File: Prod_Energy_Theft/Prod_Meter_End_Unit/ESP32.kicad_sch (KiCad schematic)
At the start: 24 parts, among them J8 U.FL-R-SMT_01_, U2 ESP32-C6-MINI-1, U4 CP2102N-Axx-xQFN20, U6 USBLC6-2SC6, U8 E32-433T20S

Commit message: PCB
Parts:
- C15, C17: footprint Footprints.kicad_mod:T491A -> Capacitor_SMD:C_0805_2012Metric
- D7, D8: footprint Footprints:LEDC2012X120N -> theftdetection:LEDC2012X120N
- J8: footprint U.FL-R-SMT_01_:HRS_U.FL-R-SMT_01_ -> theftdetection:HRS_U.FL-R-SMT_01_
- U4: footprint Package_DFN_QFN:SiliconLabs_QFN-20-1EP_3x3mm_P0.5mm -> theftdetection:IC_CP2102N-A01-GQFN20
- U8: footprint E32-433T20S:MODULE_E32-433T20S -> theftdetection:MODULE_E32-433T20S
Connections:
- net 3.3V is gone; now on net +3.3V: D7.2 (A), D8.2 (A)
- net MCB_CTRL renamed MCB_SET
- net MCB_CTRL_D renamed MCB_RESET
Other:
- sheet MCB_TD ports: added MCB_RESET, MCB_SET; removed MCB_CTRL, MCB_CTRL_D
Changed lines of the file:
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@@
 		)
 	)
-	(label "MCB_CTRL_D"
+	(label "MCB_RESET"
 		(at 270.51 147.32 0)
 		(effects
@@
 		)
 	)
-	(label "MCB_CTRL"
+	(label "MCB_SET"
 		(at 270.51 151.13 0)
 		(effects
@@
 		)
 	)
-	(label "MCB_CTRL_D"
+	(label "MCB_RESET"
 		(at 176.53 113.03 180)
 		(effects
@@
 		)
 	)
-	(label "MCB_CTRL"
+	(label "MCB_SET"
 		(at 176.53 110.49 180)
 		(effects
@@
 			)
 		)
-		(property "Footprint" "Footprints.kicad_mod:T491A"
+		(property "Footprint" "Capacitor_SMD:C_0805_2012Metric"
 			(at 118.4148 157.48 0)
 			(effects
@@
 			)
 		)
-		(property "Footprint" "U.FL-R-SMT_01_:HRS_U.FL-R-SMT_01_"
+		(property "Footprint" "theftdetection:HRS_U.FL-R-SMT_01_"
 			(at 36.83 160.02 0)
 			(effects
@@
 			)
 		)
-		(property "Footprint" "E32-433T20S:MODULE_E32-433T20S"
+		(property "Footprint" "theftdetection:MODULE_E32-433T20S"
 			(at 78.74 154.94 0)
 			(effects
@@
 			)
 		)
-		(property "Footprint" "Footprints:LEDC2012X120N"
+		(property "Footprint" "theftdetection:LEDC2012X120N"
 			(at 138.43 181.28 0)
 			(effects
@@
 			)
 		)
-		(property "Value" "3.3V"
+		(property "Value" "+3.3V"
 			(at 144.78 82.55 0)
 			(do_not_autoplace yes)
@@
 			)
 		)
-		(property "Footprint" "Footprints.kicad_mod:T491A"
+		(property "Footprint" "Capacitor_SMD:C_0805_2012Metric"
 			(at 71.12 29.5148 0)
 			(effects
@@
 			)
 		)
-		(property "Footprint" "Package_DFN_QFN:SiliconLabs_QFN-20-1EP_3x3mm_P0.5mm"
+		(property "Footprint" "theftdetection:IC_CP2102N-A01-GQFN20"
 			(at 118.11 104.14 0)
 			(effects
@@
 			)
 		)
-		(property "Footprint" "Footprints:LEDC2012X120N"
+		(property "Footprint" "theftdetection:LEDC2012X120N"
 			(at 138.43 191.44 0)
 			(effects
@@
 			)
 		)
-		(pin "MCB_CTRL" input
+		(pin "MCB_SET" input
 			(at 265.43 151.13 0)
 			(effects
@@
 			)
 		)
-		(pin "MCB_CTRL_D" input
+		(pin "MCB_RESET" input
 			(at 265.43 147.32 0)
 			(effects

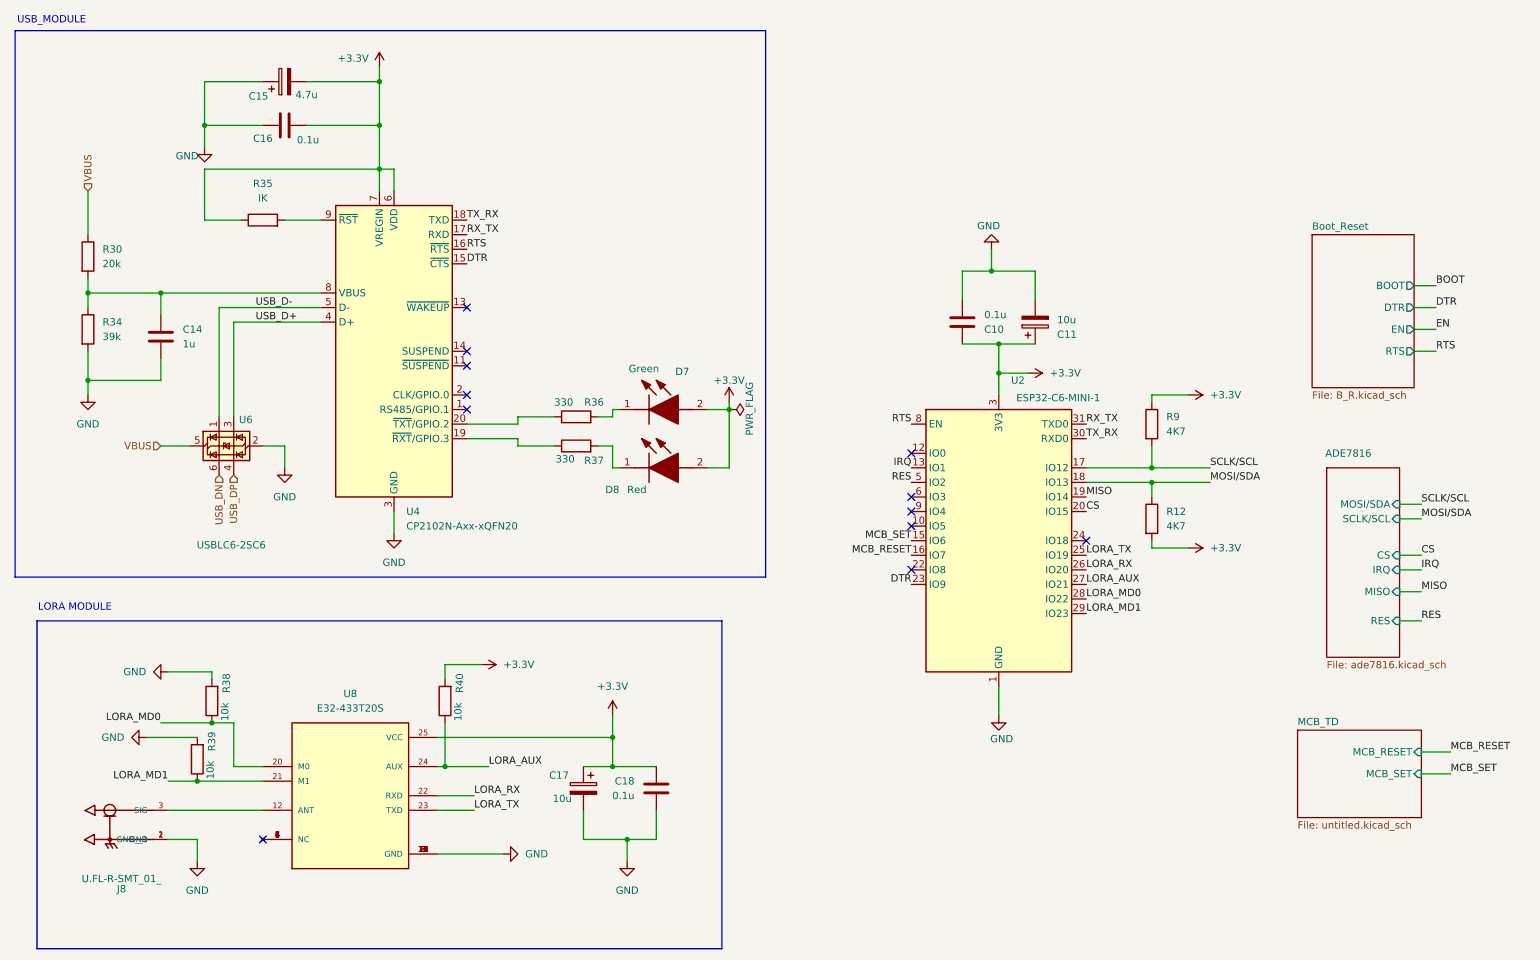
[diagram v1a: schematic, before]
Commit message: update in BOM list
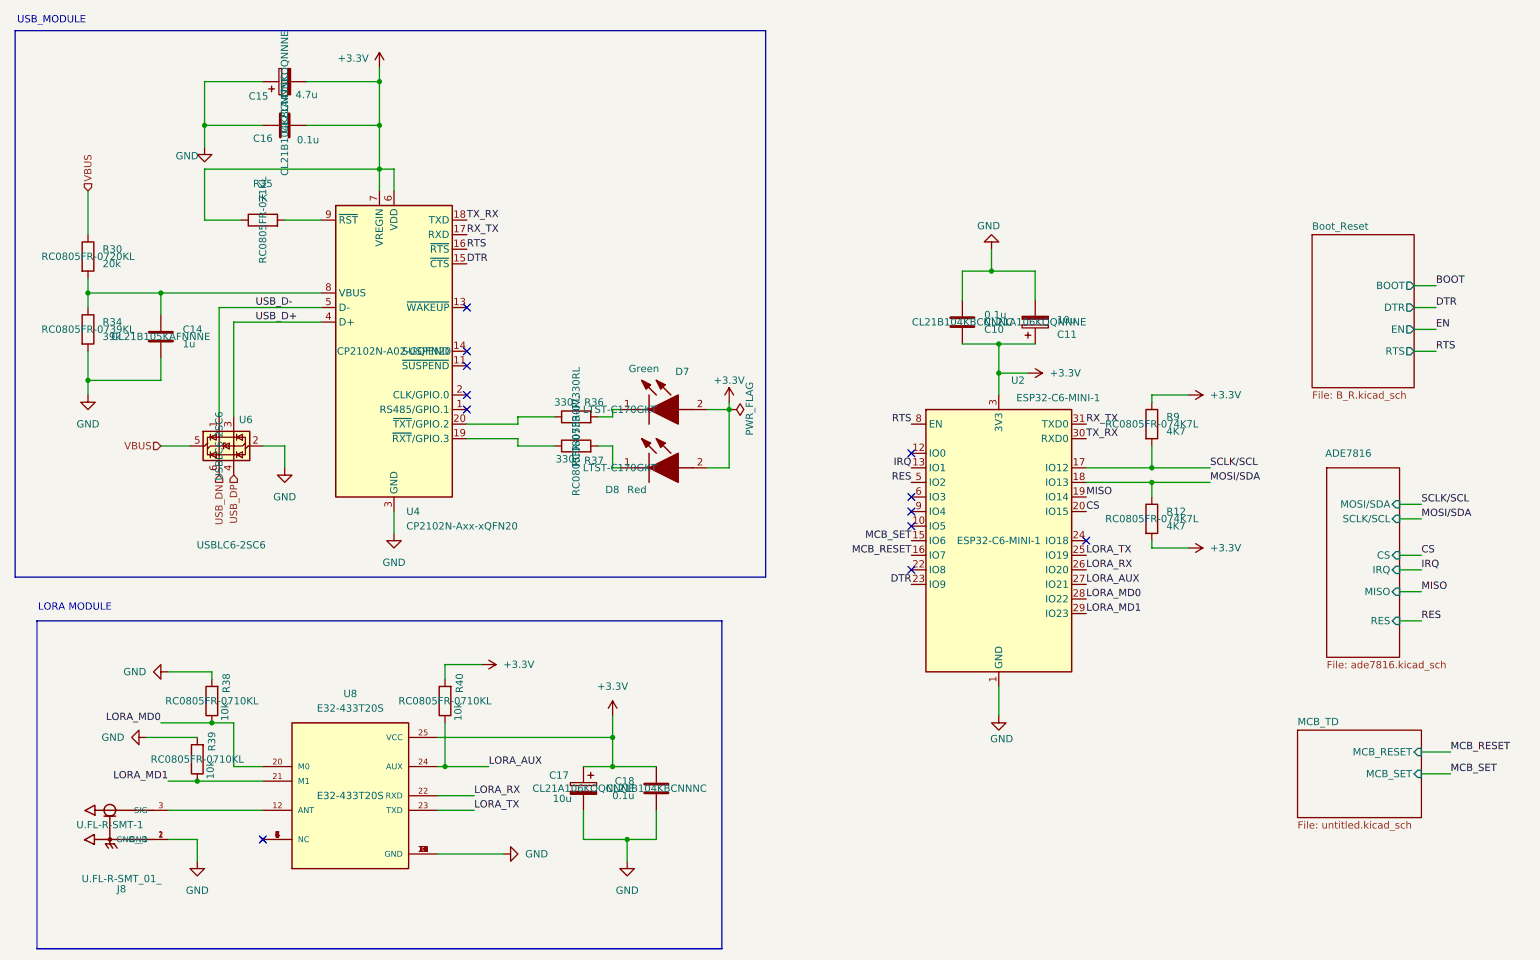
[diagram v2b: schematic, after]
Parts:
- C10, C16, C18: Part Number (none) -> CL21B104KBCNNNC
- C11, C17: Part Number (none) -> CL21A106KOQNNNE
- C14: Part Number (none) -> CL21B105KAFNNNE
- C15: Part Number (none) -> CL21A475KOQNNNE
- D7, D8: Part Number (none) -> LTST-C170GKT
- J8: Part Number (none) -> U.FL-R-SMT-1
- R12, R9: Part Number (none) -> RC0805FR-074K7L
- R30: Part Number (none) -> RC0805FR-0720KL
- R34: Part Number (none) -> RC0805FR-0739KL
- R35: Part Number (none) -> RC0805FR-071KL
- R36, R37: Part Number (none) -> RC0805FR-07330RL
- R38, R39, R40: Part Number (none) -> RC0805FR-0710KL
- U2: Part Number (none) -> ESP32-C6-MINI-1
- U4: Part Number (none) -> CP2102N-A02-GQFN20
- U6: Part Number (none) -> USBLC6-2SC6
- U8: Part Number (none) -> E32-433T20S
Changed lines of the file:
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@@
 			)
 		)
+		(property "Part Number" "RC0805FR-0739KL "
+			(at 33.02 73.66 0)
+			(effects
+				(font
+					(size 1.27 1.27)
+				)
+			)
+		)
 		(pin "2"
 		)
@@
 			)
 		)
+		(property "Part Number" "CL21A106KOQNNNE"
+			(at 119.38 153.67 0)
+			(effects
+				(font
+					(size 1.27 1.27)
+				)
+			)
+		)
 		(pin "1"
 		)
@@
 			)
 		)
+		(property "Part Number" "RC0805FR-07330RL"
+			(at 118.11 88.9 0)
+			(effects
+				(font
+					(size 1.27 1.27)
+				)
+			)
+		)
 		(pin "2"
 		)
@@
 			)
 		)
+		(property "Part Number" "U.FL-R-SMT-1 "
+			(at 36.83 160.02 0)
+			(effects
+				(font
+					(size 1.27 1.27)
+				)
+			)
+		)
 		(pin "2"
 		)
@@
 			)
 		)
+		(property "Part Number" "RC0805FR-0720KL "
+			(at 33.02 60.96 0)
+			(effects
+				(font
+					(size 1.27 1.27)
+				)
+			)
+		)
 		(pin "2"
 		)
@@
 			)
 		)
+		(property "Part Number" "E32-433T20S "
+			(at 78.74 154.94 0)
+			(effects
+				(font
+					(size 1.27 1.27)
+				)
+			)
+		)
 		(pin "4"
 		)
@@
 			)
 		)
+		(property "Part Number" "LTST-C170GKT "
+			(at 125.73 87.63 0)
+			(effects
+				(font
+					(size 1.27 1.27)
+				)
+			)
+		)
 		(pin "2"
 		)
@@
 			)
 		)
+		(property "Part Number" "CL21B104KBCNNNC "
+			(at 67.31 38.1 0)
+			(effects
+				(font
+					(size 1.27 1.27)
+				)
+			)
+		)
 		(pin "1"
 		)
@@
 			)
 		)
+		(property "Part Number" "CL21B104KBCNNNC "
+			(at 132.08 153.67 0)
+			(effects
+				(font
+					(size 1.27 1.27)
+				)
+			)
+		)
 		(pin "1"
 		)
@@
 			)
 		)
+		(property "Part Number" "CL21A475KOQNNNE "
+			(at 67.31 30.48 0)
+			(effects
+				(font
+					(size 1.27 1.27)
+				)
+			)
+		)
 		(pin "1"
 		)
@@
 			)
 		)
+		(property "Part Number" "ESP32-C6-MINI-1 "
+			(at 191.77 110.49 0)
+			(effects
+				(font
+					(size 1.27 1.27)
+				)
+			)
+		)
 		(pin "2"
 		)
@@
 			)
 		)
+		(property "Part Number" "RC0805FR-0710KL "
+			(at 95.25 138.43 0)
+			(effects
+				(font
+					(size 1.27 1.27)
+				)
+			)
+		)
 		(pin "2"
 		)
@@
 			)
 		)
+		(property "Part Number" "RC0805FR-071KL "
+			(at 63.5 54.61 0)
+			(effects
+				(font
+					(size 1.27 1.27)
+				)
+			)
+		)
 		(pin "1"
 		)
@@
 			)
 		)
+		(property "Part Number" "RC0805FR-074K7L "
+			(at 218.44 90.17 0)
+			(effects
+				(font
+					(size 1.27 1.27)
+				)
+			)
+		)
 		(pin "1"
 		)
@@
 			)
 		)
+		(property "Part Number" "CL21B105KAFNNNE "
+			(at 45.72 74.93 0)
+			(effects
+				(font
+					(size 1.27 1.27)
+				)
+			)
+		)
 		(pin "2"
 		)
@@
 			)
 		)
+		(property "Part Number" "RC0805FR-0710KL "
+			(at 54.61 138.43 0)
+			(effects
+				(font
+					(size 1.27 1.27)
+				)
+			)
+		)
 		(pin "2"
 		)
@@
 			)
 		)
+		(property "Part Number" "CP2102N-A02-GQFN20 "
+			(at 86.36 77.47 0)
+			(effects
+				(font
+					(size 1.27 1.27)
+				)
+			)
+		)
 		(pin "3"
 		)
@@
 			)
 		)
+		(property "Part Number" "LTST-C170GKT "
+			(at 125.73 97.79 0)
+			(effects
+				(font
+					(size 1.27 1.27)
+				)
+			)
+		)
 		(pin "2"
 		)
@@
 			)
 		)
+		(property "Part Number" "CL21A106KOQNNNE"
+			(at 198.12 72.39 0)
+			(effects
+				(font
+					(size 1.27 1.27)
+				)
+			)
+		)
 		(pin "1"
 		)
@@
 			)
 		)
+		(property "Part Number" "USBLC6-2SC6 "
+			(at 55.88 93.98 0)
+			(effects
+				(font
+					(size 1.27 1.27)
+				)
+			)
+		)
 		(pin "4"
 		)
@@
 			)
 		)
+		(property "Part Number" "RC0805FR-074K7L "
+			(at 218.44 106.68 0)
+			(effects
+				(font
+					(size 1.27 1.27)
+				)
+			)
+		)
 		(pin "1"
 		)
@@
 			)
 		)
+		(property "Part Number" "CL21B104KBCNNNC "
+			(at 185.42 72.39 0)
+			(effects
+				(font
+					(size 1.27 1.27)
+				)
+			)
+		)
 		(pin "1"
 		)
@@
 			)
 		)
+		(property "Part Number" "RC0805FR-07330RL"
+			(at 118.11 93.98 0)
+			(effects
+				(font
+					(size 1.27 1.27)
+				)
+			)
+		)
 		(pin "2"
 		)
@@
 			)
 		)
+		(property "Part Number" "RC0805FR-0710KL "
+			(at 52.07 148.59 0)
+			(effects
+				(font
+					(size 1.27 1.27)
+				)
+			)
+		)
